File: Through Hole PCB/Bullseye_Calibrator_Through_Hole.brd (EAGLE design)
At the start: 50.8 x 83.8 mm, 16 parts, among them IC1 78L15

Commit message: Add files via upload
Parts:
- added J3: (no value), jumper:JP1
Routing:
- net S$61: track 0.00 -> 35.7 mm
- net S$57: track 60.1 -> 24.7 mm
- net S$62: track 0.00 -> 18.6 mm
- net S$60: track 0.00 -> 15.7 mm
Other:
- board text added: "25 MHz Out"
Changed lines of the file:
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@@
 G4EML</text>
 <text x="14.365821875" y="26.578703125" size="1.778" layer="21" font="fixed">ARDUINO NANO</text>
+<text x="41.45064375" y="76.44145625" size="1.778" layer="21" align="center">25
+MHz
+Out</text>
 </plain>
 <attributes>
@@
 <attribute name="NAME" x="40.437653125" y="69.51491875" size="1.27" layer="25" ratio="10" rot="R180"/>
 </element>
+<element name="J3" library="jumper" package="JP1" value="" x="45.25555625" y="76.40835625" smashed="yes">
+<attribute name="NAME" x="46.353590625" y="81.00411875" size="1.27" layer="25" ratio="10" rot="R180"/>
+<attribute name="VALUE" x="48.17655625" y="73.86835625" size="1.27" layer="27" ratio="10" rot="R90"/>
+</element>
 </elements>
 <signals>
@@
 <wire x1="25.2882625" y1="66.160090625" x2="23.17899375" y2="66.160090625" width="1.27" layer="16"/>
 </signal>
+<signal name="S$60">
+<wire x1="43.179359375" y1="66.1044125" x2="43.2274" y2="50.442665625" width="1.6764" layer="16"/>
+</signal>
 <signal name="S$57">
 <wire x1="21.175271875" y1="71.945178125" x2="21.175271875" y2="80.2086" width="1.6764" layer="16"/>
@@
 <wire x1="21.25105625" y1="80.094884375" x2="29.246228125" y2="80.094884375" width="1.6764" layer="16"/>
 <wire x1="29.246228125" y1="80.094884375" x2="29.246228125" y2="71.87108125" width="1.6764" layer="16"/>
-<wire x1="29.246228125" y1="71.87108125" x2="43.2274" y2="71.87108125" width="1.6764" layer="16"/>
-<wire x1="43.2274" y1="71.87108125" x2="43.2274" y2="50.442665625" width="1.6764" layer="16"/>
 </signal>
 <signal name="S$58">
@@
 <wire x1="32.4428375" y1="66.1208625" x2="35.70490625" y2="66.1208625" width="1.27" layer="16"/>
 </signal>
+<signal name="S$61">
+<wire x1="43.23779375" y1="66.1244625" x2="48.3782875" y2="66.1244625" width="1.6764" layer="16"/>
+<wire x1="48.3782875" y1="66.1244625" x2="48.3782875" y2="77.60974375" width="1.6764" layer="16"/>
+<wire x1="48.3782875" y1="77.60974375" x2="29.35365625" y2="77.60974375" width="1.6764" layer="16"/>
+<wire x1="29.35365625" y1="77.60974375" x2="29.35365625" y2="77.561690625" width="1.6764" layer="16"/>
+</signal>
+<signal name="S$62">
+<wire x1="45.27958125" y1="75.0398875" x2="35.631146875" y2="75.0398875" width="1.6764" layer="16"/>
+<wire x1="35.631146875" y1="75.0398875" x2="35.631146875" y2="66.0703375" width="1.6764" layer="16"/>
+</signal>
 </signals>

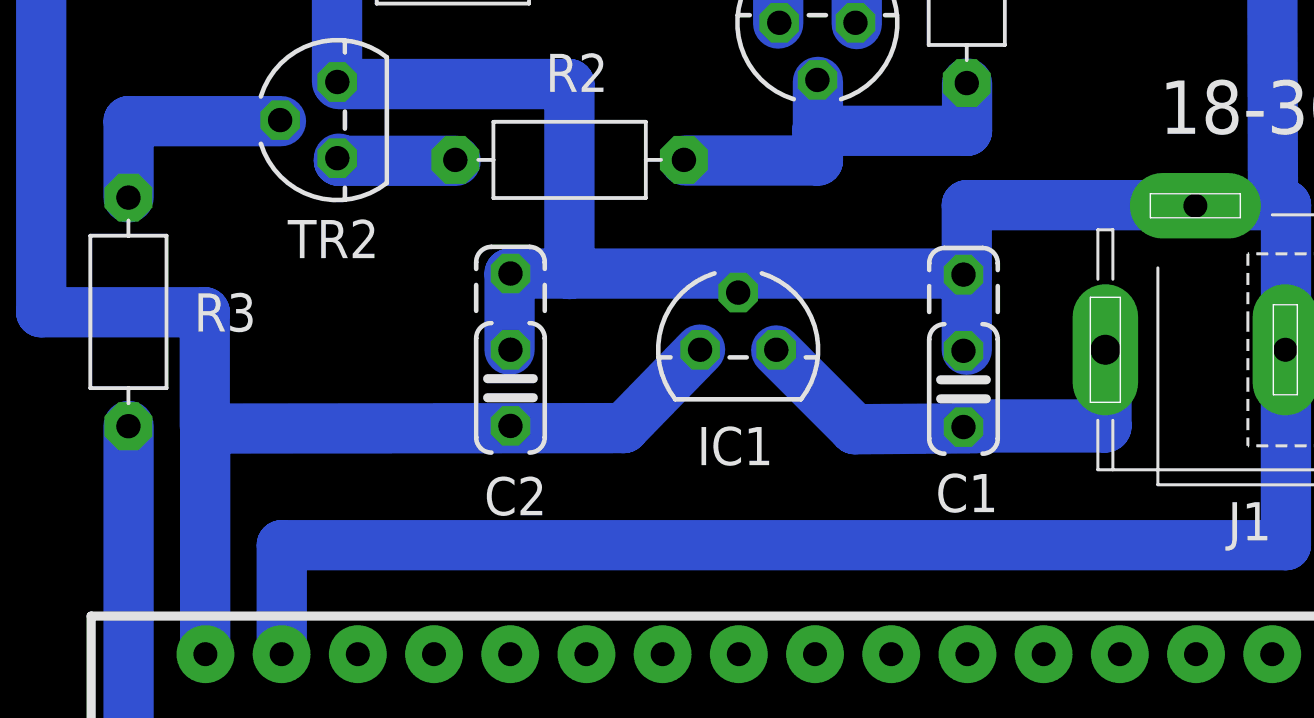
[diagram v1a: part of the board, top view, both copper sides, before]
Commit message: Add Input Diode
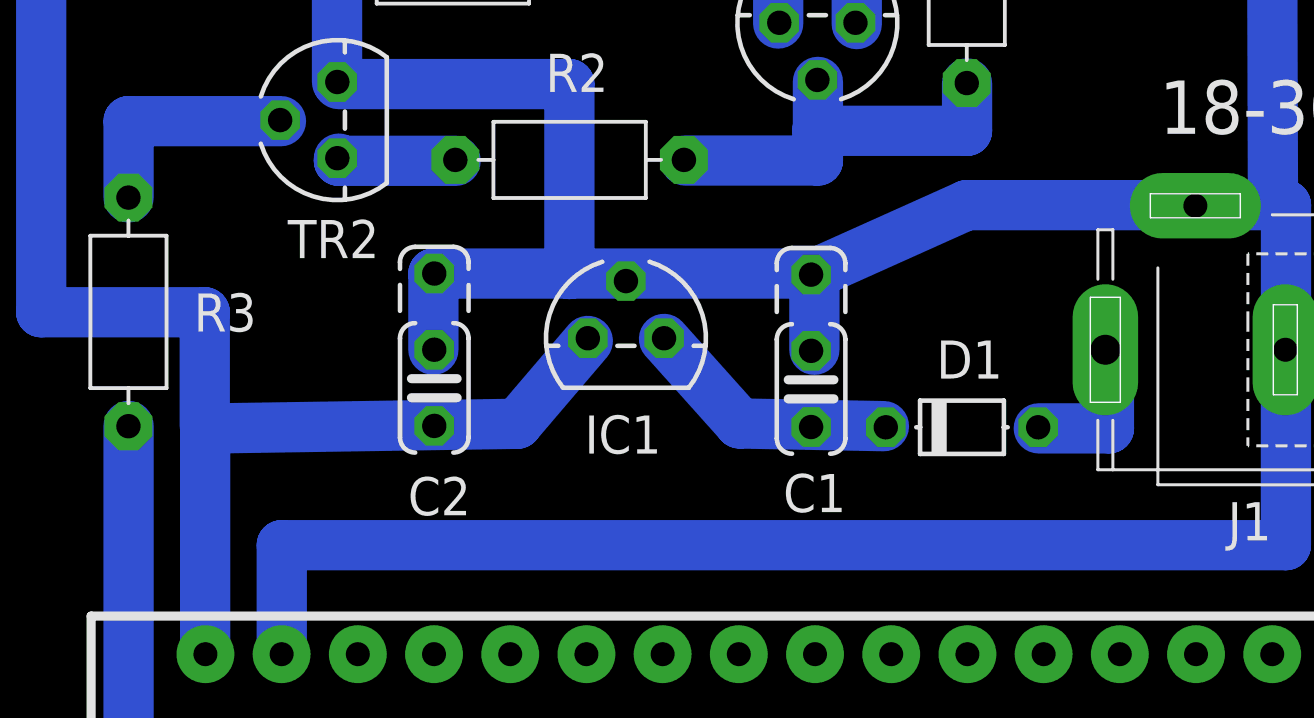
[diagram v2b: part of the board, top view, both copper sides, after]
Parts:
- added D1: (no value), ref-packages:D-5
- moved C1 5.08 mm to (27.8, 44.4)
- moved IC1 3.76 mm to (21.7, 46.1)
- moved C2 2.54 mm to (15.3, 44.5)
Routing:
- net D1: track 0.00 -> 8.59 mm
- net S$45: track 7.16 -> 0.00 mm
- net S$42: track 25.1 -> 21.6 mm
- net S$43: track 7.76 -> 4.70 mm
- net S$44: track 39.3 -> 40.0 mm
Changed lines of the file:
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@@
 <element name="S2" library="switch-omron" package="B3F-10XX" value="" x="25.397153125" y="9.433584375" rot="R90"/>
 <element name="S3" library="switch-omron" package="B3F-10XX" value="" x="42.885275" y="9.423371875" rot="R90"/>
-<element name="IC1" library="linear" package="TO92" value="78L15" x="25.4" y="45.72" smashed="yes">
-<attribute name="NAME" x="24.023821875" y="41.874684375" size="1.27" layer="25" ratio="10"/>
+<element name="IC1" library="linear" package="TO92" value="78L15" x="21.65895" y="46.10444375" smashed="yes">
+<attribute name="NAME" x="20.282771875" y="42.259128125" size="1.27" layer="25" ratio="10"/>
 </element>
 <element name="TR2" library="linear" package="TO92" value="NPN" x="12.037575" y="53.375684375" smashed="yes" rot="R90">
@@
 <attribute name="NAME" x="30.059446875" y="67.86946875" size="1.27" layer="25" ratio="10"/>
 </element>
-<element name="C2" library="rcl" package="C025_050-024X070" value="100n" x="17.810021875" y="44.45126875" smashed="yes" rot="R270">
-<attribute name="NAME" x="16.933375" y="40.20400625" size="1.27" layer="25" ratio="10"/>
-</element>
-<element name="C1" library="rcl" package="C025_050-024X070" value="100n" x="32.910259375" y="44.41428125" smashed="yes" rot="R270">
-<attribute name="NAME" x="31.9817875" y="40.3086" size="1.27" layer="25" ratio="10"/>
+<element name="C2" library="rcl" package="C025_050-024X070" value="100n" x="15.270021875" y="44.45126875" smashed="yes" rot="R270">
+<attribute name="NAME" x="14.393375" y="40.20400625" size="1.27" layer="25" ratio="10"/>
+</element>
+<element name="C1" library="rcl" package="C025_050-024X070" value="100n" x="27.830259375" y="44.41428125" smashed="yes" rot="R270">
+<attribute name="NAME" x="26.9017875" y="40.3086" size="1.27" layer="25" ratio="10"/>
 </element>
 <element name="J1" library="con-jack" package="SPC4077" value="" x="40.64" y="45.72" smashed="yes" rot="R180">
@@
 <attribute name="NAME" x="46.353590625" y="81.00411875" size="1.27" layer="25" ratio="10" rot="R180"/>
 <attribute name="VALUE" x="48.17655625" y="73.86835625" size="1.27" layer="27" ratio="10" rot="R90"/>
+</element>
+<element name="D1" library="ref-packages" package="D-5" value="" x="32.860103125" y="43.136025" smashed="yes">
+<attribute name="NAME" x="32.009803125" y="44.759534375" size="1.27" layer="25" ratio="10"/>
+<attribute name="VALUE" x="31.209103125" y="40.723025" size="1.27" layer="27" ratio="10"/>
 </element>
 </elements>
@@
 </signal>
 <signal name="S$42">
-<wire x1="24.12981875" y1="45.7255125" x2="21.582778125" y2="43.108215625" width="1.6764" layer="16"/>
-<wire x1="21.582778125" y1="43.108215625" x2="7.632515625" y2="43.093853125" width="1.6764" layer="16"/>
+<wire x1="20.38876875" y1="46.013846875" x2="18.03389375" y2="43.25238125" width="1.6764" layer="16"/>
+<wire x1="18.03389375" y1="43.25238125" x2="7.632515625" y2="43.093853125" width="1.6764" layer="16"/>
 <wire x1="7.632515625" y1="43.093853125" x2="7.632515625" y2="35.56" width="1.6764" layer="16"/>
 <wire x1="7.632515625" y1="35.56" x2="7.62" y2="35.56" width="1.778" layer="16"/>
 </signal>
-<signal name="S$43">
-<wire x1="26.66824375" y1="45.696421875" x2="29.288646875" y2="43.0703375" width="1.6764" layer="16"/>
-<wire x1="29.288646875" y1="43.0703375" x2="33.336184375" y2="43.10191875" width="1.6764" layer="16"/>
+<signal name="D1">
+<wire x1="22.92719375" y1="46.080865625" x2="25.4515125" y2="43.262559375" width="1.6764" layer="16"/>
+<wire x1="25.4515125" y1="43.262559375" x2="30.25859375" y2="43.17331875" width="1.6764" layer="16"/>
 </signal>
 <signal name="S$44">
-<wire x1="33.02" y1="45.72" x2="33.02" y2="48.26" width="1.6764" layer="16"/>
-<wire x1="33.02" y1="48.26" x2="17.78" y2="48.26" width="1.6764" layer="16"/>
-<wire x1="17.78" y1="48.26" x2="17.78" y2="45.72" width="1.6764" layer="16"/>
-<wire x1="33.02" y1="48.26" x2="33.02" y2="50.54051875" width="1.6764" layer="16"/>
+<wire x1="27.94" y1="45.72" x2="27.94" y2="48.26" width="1.6764" layer="16"/>
+<wire x1="27.94" y1="48.26" x2="15.24" y2="48.26" width="1.6764" layer="16"/>
+<wire x1="15.24" y1="48.26" x2="15.24" y2="45.72" width="1.6764" layer="16"/>
+<wire x1="27.94" y1="48.26" x2="33.02" y2="50.54051875" width="1.6764" layer="16"/>
 <wire x1="33.02" y1="50.54051875" x2="43.661440625" y2="50.54051875" width="1.6764" layer="16"/>
 <wire x1="43.661440625" y1="50.54051875" x2="43.661440625" y2="44.5760875" width="1.6764" layer="16"/>
 <wire x1="43.661440625" y1="44.5760875" x2="43.705284375" y2="44.5760875" width="1.778" layer="16"/>
-</signal>
-<signal name="S$45">
-<wire x1="37.626753125" y1="45.73158125" x2="37.626753125" y2="43.18" width="1.778" layer="16"/>
-<wire x1="37.626753125" y1="43.18" x2="33.02" y2="43.18" width="1.778" layer="16"/>
 </signal>
 <signal name="S$46">
@@
 <wire x1="35.631146875" y1="75.0398875" x2="35.631146875" y2="66.0703375" width="1.6764" layer="16"/>
 </signal>
+<signal name="S$43">
+<wire x1="35.419790625" y1="43.10005" x2="37.759490625" y2="43.10005" width="1.6764" layer="16"/>
+<wire x1="37.759490625" y1="43.10005" x2="37.759490625" y2="45.46233125" width="1.6764" layer="16"/>
+</signal>
 </signals>
